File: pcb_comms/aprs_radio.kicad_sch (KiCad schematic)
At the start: 33 parts, among them J5 SMA_CONN, Q1 DTC144EET1G, U3 DRA818V

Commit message: Add UART USB
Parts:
- Q1: footprint SOT50P160X90-3N -> TRANSISTOR_DTC144EET1G:TRANSISTOR_DTC144EET1G
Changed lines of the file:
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@@
 			)
 		)
-		(property "Footprint" "SOT50P160X90-3N"
+		(property "Footprint" "TRANSISTOR_DTC144EET1G:TRANSISTOR_DTC144EET1G"
 			(at 57.15 220.65 0)
 			(effects

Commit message: Update pinout
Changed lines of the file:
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@@
+	)
+	(junction
+		(at 66.04 168.91)
+		(diameter 0)
+		(color 0 0 0 0)
 	)
 	(junction
@@
 	(wire
 		(pts
-			(xy 71.12 168.91) (xy 58.42 168.91)
+			(xy 71.12 168.91) (xy 66.04 168.91)
 		)
 		(stroke
@@
 		(pts
 			(xy 45.72 168.91) (xy 58.42 168.91)
+		)
+		(stroke
+			(width 0)
+			(type default)
+		)
+	)
+	(wire
+		(pts
+			(xy 66.04 168.91) (xy 58.42 168.91)
 		)
 		(stroke
@@
 					(unit 1)
 				)
+			)
+		)
+	)
+	(symbol
+		(lib_id "power:PWR_FLAG")
+		(at 66.04 168.91 0)
+		(unit 1)
+		(exclude_from_sim no)
+		(in_bom yes)
+		(on_board yes)
+		(dnp no)
+		(property "Reference" "#FLG03"
+			(at 66.04 167.005 0)
+			(effects
+				(font
+					(size 1.27 1.27)
+				)
+				(hide yes)
+			)
+		)
+		(property "Value" "PWR_FLAG"
+			(at 66.04 165.1 0)
+			(effects
+				(font
+					(size 1.27 1.27)
+				)
+			)
+		)
+		(property "Footprint" ""
+			(at 66.04 168.91 0)
+			(effects
+				(font
+					(size 1.27 1.27)
+				)
+				(hide yes)
+			)
+		)
+		(property "Datasheet" "~"
+			(at 66.04 168.91 0)
+			(effects
+				(font
+					(size 1.27 1.27)
+				)
+				(hide yes)
+			)
+		)
+		(property "Description" "Special symbol for telling ERC where power comes from"
+			(at 66.04 168.91 0)
+			(effects
+				(font
+					(size 1.27 1.27)
+				)
+				(hide yes)
+			)
+		)
+		(pin "1"
+		)
+		(instances
+			(project ""
+				(path "/ea597178-b44d-4db9-826c-8f86e8d231f0/30ba8b84-3a26-43d9-a2eb-61726928da4d"
+					(reference "#FLG03")
+					(unit 1)
+				)

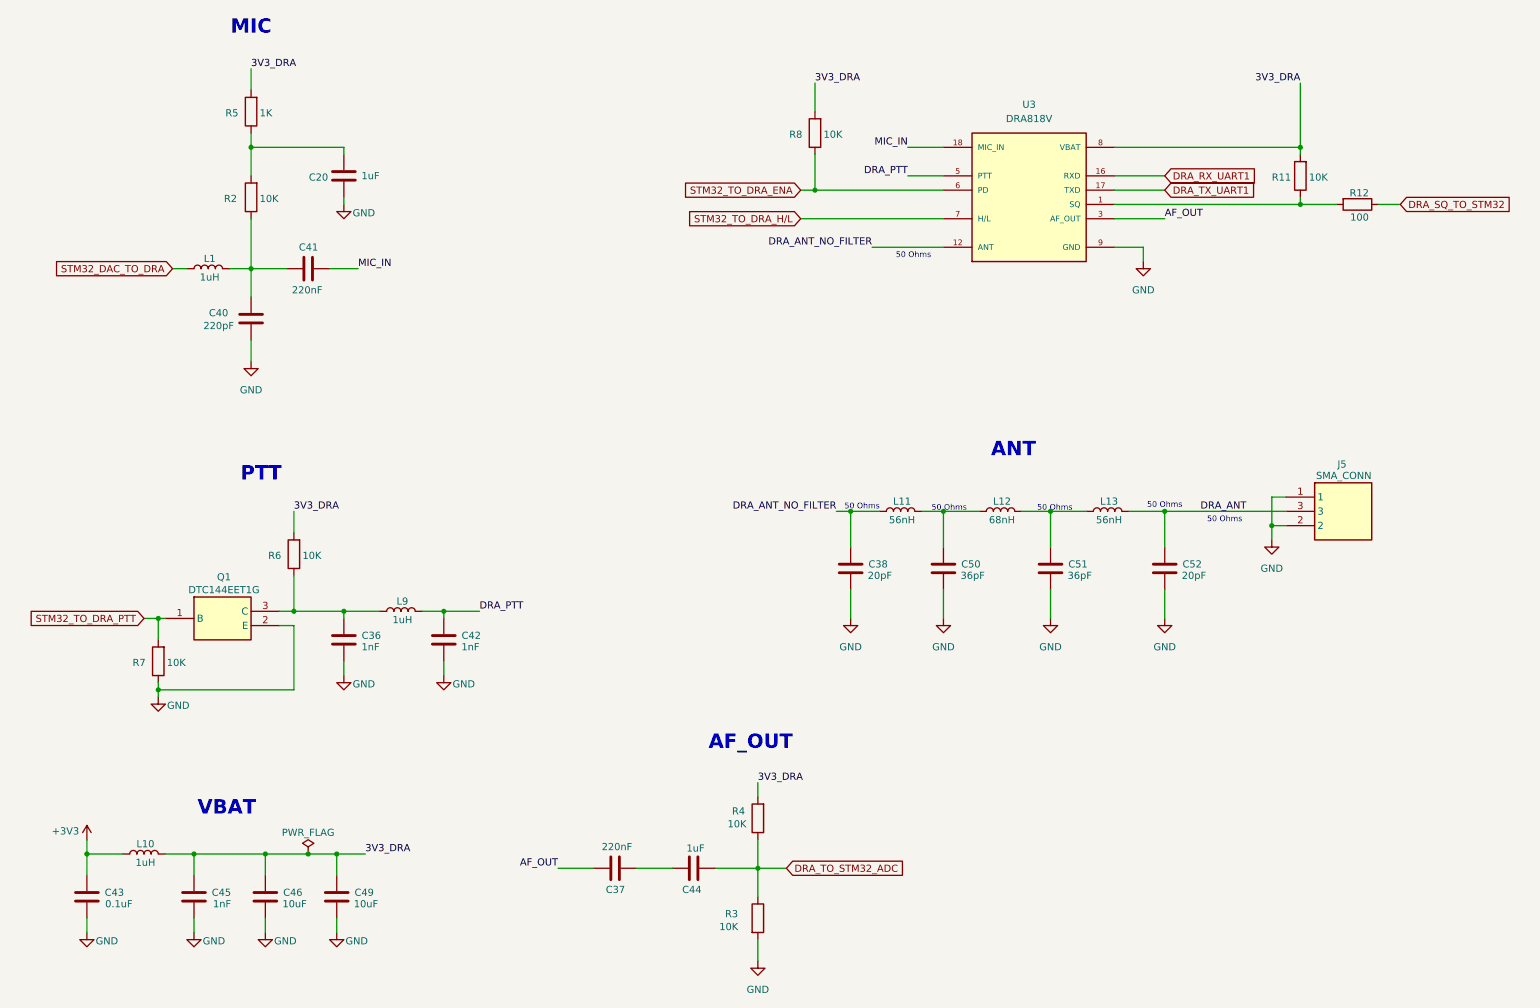
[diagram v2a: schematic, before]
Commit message: Update schematic. Add net classes and JST footprints for aux
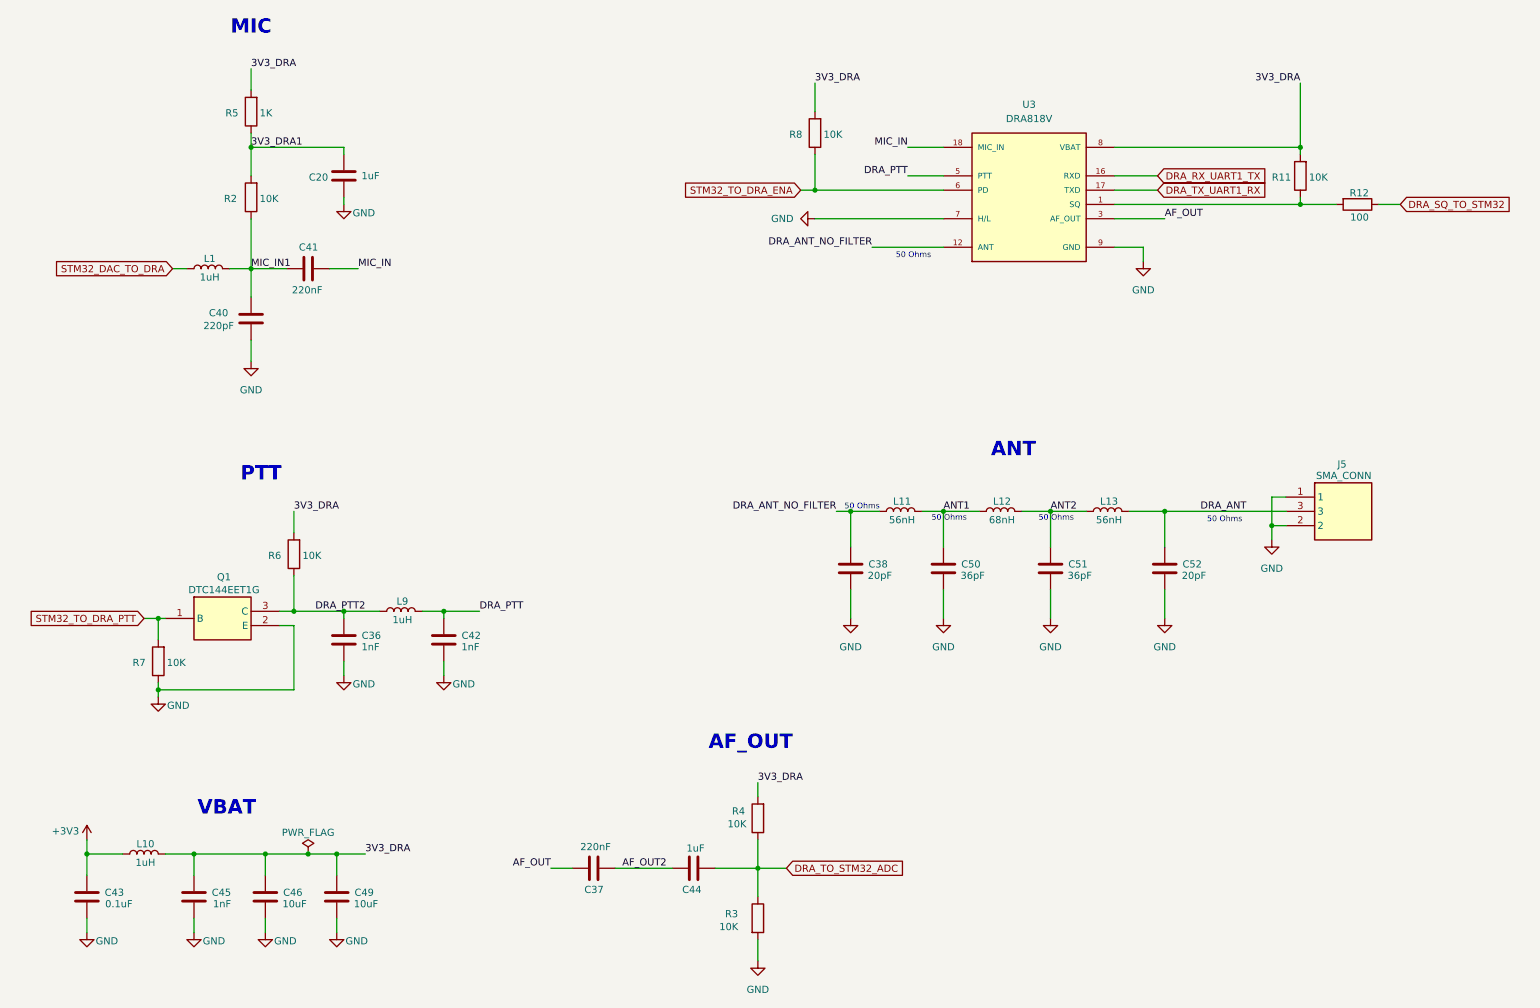
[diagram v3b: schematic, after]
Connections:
- net STM32_TO_DRA_H/L is gone; now on net GND: U3.7 (H/L)
- net MIC_IN1: now reaches C40.1, C41.1, L1.2, R2.1
- net DRA_PTT2: now reaches C36.1, L9.1, Q1.3 (C), R6.1
- net 3V3_DRA1: now reaches C20.1, R2.2, R5.1
- net AF_OUT2: now reaches C37.2, C44.2
- net ANT1: now reaches C50.1, L11.2, L12.1
- net ANT2: now reaches C51.1, L12.2, L13.1
- net DRA_RX_UART1 renamed DRA_RX_UART1_TX
- net DRA_TX_UART1 renamed DRA_TX_UART1_RX
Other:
- moved on the sheet: C37
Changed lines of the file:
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@@
 	(text "50 Ohms"
 		(exclude_from_sim no)
-		(at 180.086 107.442 0)
+		(at 180.086 109.22 0)
 		(effects
 			(font
@@
 	(text "50 Ohms"
 		(exclude_from_sim no)
-		(at 198.882 107.442 0)
-		(effects
-			(font
-				(size 1.016 1.016)
-				(color 255 0 0 1)
-			)
-		)
-	)
-	(text "50 Ohms"
-		(exclude_from_sim no)
-		(at 218.44 106.934 0)
+		(at 199.136 109.22 0)
 		(effects
 			(font
@@
 	(wire
 		(pts
+			(xy 156.21 55.88) (xy 179.07 55.88)
+		)
+		(stroke
+			(width 0)
+			(type default)
+		)
+	)
+	(wire
+		(pts
 			(xy 237.49 110.49) (xy 237.49 113.03)
 		)
@@
 	(wire
 		(pts
-			(xy 110.49 171.45) (xy 116.84 171.45)
+			(xy 109.22 171.45) (xy 113.03 171.45)
 		)
 		(stroke
@@
 	(wire
 		(pts
-			(xy 124.46 171.45) (xy 130.81 171.45)
-		)
-		(stroke
-			(width 0)
-			(type default)
-		)
-	)
-	(wire
-		(pts
 			(xy 153.67 50.8) (xy 156.21 50.8)
 		)
@@
 	(wire
 		(pts
-			(xy 209.55 50.8) (xy 218.44 50.8)
+			(xy 156.21 50.8) (xy 179.07 50.8)
 		)
 		(stroke
@@
 	(wire
 		(pts
-			(xy 156.21 50.8) (xy 179.07 50.8)
+			(xy 242.57 53.34) (xy 248.92 53.34)
 		)
 		(stroke
@@
 	(wire
 		(pts
-			(xy 242.57 53.34) (xy 248.92 53.34)
+			(xy 120.65 171.45) (xy 130.81 171.45)
 		)
 		(stroke
@@
 	(wire
 		(pts
-			(xy 71.12 180.34) (xy 71.12 182.88)
+			(xy 209.55 48.26) (xy 217.17 48.26)
 		)
 		(stroke
@@
 	(wire
 		(pts
-			(xy 153.67 55.88) (xy 179.07 55.88)
+			(xy 71.12 180.34) (xy 71.12 182.88)
 		)
 		(stroke
@@
 	(wire
 		(pts
-			(xy 209.55 48.26) (xy 218.44 48.26)
-		)
-		(stroke
-			(width 0)
-			(type default)
-		)
-	)
-	(wire
-		(pts
 			(xy 90.17 134.62) (xy 90.17 137.16)
 		)
@@
 	(wire
 		(pts
+			(xy 209.55 50.8) (xy 217.17 50.8)
+		)
+		(stroke
+			(width 0)
+			(type default)
+		)
+	)
+	(wire
+		(pts
 			(xy 179.07 107.95) (xy 185.42 107.95)
 		)
@@
 		)
 	)
+	(label "ANT2"
+		(at 198.12 107.95 0)
+		(effects
+			(font
+				(size 1.27 1.27)
+			)
+			(justify left bottom)
+		)
+	)
+	(label "ANT1"
+		(at 179.07 107.95 0)
+		(effects
+			(font
+				(size 1.27 1.27)
+			)
+			(justify left bottom)
+		)
+	)
 	(label "DRA_ANT_NO_FILTER"
 		(at 166.37 60.96 180)
@@
 		)
 	)
+	(label "3V3_DRA1"
+		(at 55.88 43.18 0)
+		(effects
+			(font
+				(size 1.27 1.27)
+			)
+			(justify left bottom)
+		)
+	)
 	(label "DRA_PTT"
 		(at 172.72 48.26 180)
@@
 		)
 	)
+	(label "AF_OUT2"
+		(at 121.92 171.45 0)
+		(effects
+			(font
+				(size 1.27 1.27)
+			)
+			(justify left bottom)
+		)
+	)
 	(label "AF_OUT"
-		(at 110.49 171.45 180)
+		(at 109.22 171.45 180)
 		(effects
 			(font
@@
 		)
 	)
+	(label "DRA_PTT2"
+		(at 67.31 125.73 0)
+		(effects
+			(font
+				(size 1.27 1.27)
+			)
+			(justify left bottom)
+		)
+	)
 	(label "3V3_DRA"
 		(at 63.5 107.95 0)
@@
 		)
 	)
+	(label "MIC_IN1"
+		(at 55.88 64.77 0)
+		(effects
+			(font
+				(size 1.27 1.27)
+			)
+			(justify left bottom)
+		)
+	)
 	(label "AF_OUT"
 		(at 218.44 55.88 0)
@@
 		)
 	)
-	(global_label "DRA_TX_UART1"
-		(shape input)
-		(at 218.44 50.8 0)
-		(fields_autoplaced yes)
-		(effects
-			(font
-				(size 1.27 1.27)
-			)
-			(justify left)
-		)
-		(property "Intersheetrefs" "${INTERSHEET_REFS}"
-			(at 235.0323 50.8 0)
-			(effects
-				(font
-					(size 1.27 1.27)
-				)
-				(justify left)
-				(hide yes)
-			)
-		)
-	)
 	(global_label "STM32_TO_DRA_PTT"
 		(shape input)
@@
 		)
 	)
-	(global_label "STM32_TO_DRA_ENA"
+	(global_label "DRA_RX_UART1_TX"
 		(shape input)
-		(at 153.67 50.8 180)
+		(at 217.17 48.26 0)
 		(fields_autoplaced yes)
 		(effects
@@
 				(size 1.27 1.27)
 			)
-			(justify right)
+			(justify left)
 		)
 		(property "Intersheetrefs" "${INTERSHEET_REFS}"
-			(at 132.2397 50.8 0)
+			(at 237.2094 48.26 0)
 			(effects
 				(font
 					(size 1.27 1.27)
 				)
-				(justify right)
+				(justify left)
 				(hide yes)
 			)
 		)
 	)
-	(global_label "DRA_RX_UART1"
+	(global_label "DRA_TX_UART1_RX"
 		(shape input)
-		(at 218.44 48.26 0)
+		(at 217.17 50.8 0)
 		(fields_autoplaced yes)
 		(effects
@@
 		)
 		(property "Intersheetrefs" "${INTERSHEET_REFS}"
-			(at 235.3347 48.26 0)
+			(at 237.2094 50.8 0)
 			(effects
 				(font
@@
 		)
 	)
-	(global_label "STM32_TO_DRA_H{slash}L"
+	(global_label "STM32_TO_DRA_ENA"
 		(shape input)
-		(at 153.67 55.88 180)
+		(at 153.67 50.8 180)
 		(fields_autoplaced yes)
 		(effects
@@
 		)
 		(property "Intersheetrefs" "${INTERSHEET_REFS}"
-			(at 132.1187 55.88 0)
+			(at 132.2397 50.8 0)
 			(effects
 				(font
@@
 	(symbol
 		(lib_id "power:GND")
+		(at 156.21 55.88 270)
+		(unit 1)
+		(exclude_from_sim no)
+		(in_bom yes)
+		(on_board yes)
+		(dnp no)
+		(fields_autoplaced yes)
+		(property "Reference" "#PWR060"
+			(at 149.86 55.88 0)
+			(effects
+				(font
+					(size 1.27 1.27)
+				)
+				(hide yes)
+			)
+		)
+		(property "Value" "GND"
+			(at 152.4 55.8799 90)
+			(effects
+				(font
+					(size 1.27 1.27)
+				)
+				(justify right)
+			)
+		)
+		(property "Footprint" ""
+			(at 156.21 55.88 0)
+			(effects
+				(font
+					(size 1.27 1.27)
+				)
+				(hide yes)
+			)
+		)
+		(property "Datasheet" ""
+			(at 156.21 55.88 0)
+			(effects
+				(font
+					(size 1.27 1.27)
+				)
+				(hide yes)
+			)
+		)
+		(property "Description" "Power symbol creates a global label with name \"GND\" , ground"
+			(at 156.21 55.88 0)
+			(effects
+				(font
+					(size 1.27 1.27)
+				)
+				(hide yes)
+			)
+		)
+		(pin "1"
+		)
+		(instances
+			(project "pcb_comms_board"
+				(path "/ea597178-b44d-4db9-826c-8f86e8d231f0/30ba8b84-3a26-43d9-a2eb-61726928da4d"
+					(reference "#PWR060")
+					(unit 1)
+				)
+			)
+		)
+	)
+	(symbol
+		(lib_id "power:GND")
 		(at 214.63 63.5 0)
 		(unit 1)
@@
 	(symbol
 		(lib_id "Device:C")
-		(at 120.65 171.45 90)
+		(at 116.84 171.45 90)
 		(unit 1)
 		(exclude_from_sim no)
@@
 		(dnp no)
 		(property "Reference" "C37"
-			(at 122.428 175.26 90)
+			(at 118.618 175.26 90)
 			(effects
 				(font
@@
 		)
 		(property "Value" "220nF"
-			(at 123.698 167.64 90)
+			(at 119.888 167.64 90)
 			(effects
 				(font
@@
 		)
 		(property "Footprint" "Capacitor_SMD:C_0805_2012Metric_Pad1.18x1.45mm_HandSolder"
-			(at 124.46 170.4848 0)
+			(at 120.65 170.4848 0)
 			(effects
 				(font
@@
 		)
 		(property "Datasheet" "~"
-			(at 120.65 171.45 0)
+			(at 116.84 171.45 0)
 			(effects
 				(font
@@
 		)
 		(property "Description" "Unpolarized capacitor"
-			(at 120.65 171.45 0)
+			(at 116.84 171.45 0)
 			(effects
 				(font
@@
 		)
 		(property "KLC_S3.3" ""
-			(at 120.65 171.45 90)
+			(at 116.84 171.45 90)
 			(effects
 				(font
@@
 		)
 		(property "KLC_S4.1" ""
-			(at 120.65 171.45 90)
+			(at 116.84 171.45 90)
 			(effects
 				(font

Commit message: Version 1.1
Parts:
- removed J5: SMA_CONN, SMA_ANTENNA_CONSMA002-SMD-G:SMA_ANTENNA_CONSMA002-SMD-G, symbol SMA_ANTENNA_CONSMA002-SMD-G:CONSMA002-SMD-G
- added J4: SMA_CONNECTOR, SMA_ANTENNA_VERTICAL:LPRS_SMA_CONNECTOR, symbol SMA_CONNECTOR:SMA_CONNECTOR
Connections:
- net DRA_ANT: now also J4.1
- net GND: now also J4.G1, J4.G2, J4.G3, J4.G4
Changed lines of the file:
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@@
 	)
 	(junction
-		(at 237.49 110.49)
-		(diameter 0)
-		(color 0 0 0 0)
-	)
-	(junction
 		(at 39.37 139.7)
 		(diameter 0)
@@
 	(wire
 		(pts
-			(xy 240.03 110.49) (xy 237.49 110.49)
+			(xy 237.49 110.49) (xy 241.3 110.49)
 		)
 		(stroke
@@
 	(wire
 		(pts
-			(xy 218.44 107.95) (xy 240.03 107.95)
+			(xy 218.44 107.95) (xy 241.3 107.95)
 		)
 		(stroke
@@
 	(wire
 		(pts
-			(xy 240.03 105.41) (xy 237.49 105.41)
-		)
-		(stroke
-			(width 0)
-			(type default)
-		)
-	)
-	(wire
-		(pts
-			(xy 237.49 105.41) (xy 237.49 110.49)
-		)
-		(stroke
-			(width 0)
-			(type default)
-		)
-	)
-	(wire
-		(pts
 			(xy 63.5 119.38) (xy 63.5 125.73)
 		)
@@
 	)
 	(symbol
-		(lib_id "SMA_ANTENNA_CONSMA002-SMD-G:CONSMA002-SMD-G")
-		(at 240.03 105.41 0)
-		(unit 1)
-		(exclude_from_sim no)
-		(in_bom yes)
-		(on_board yes)
-		(dnp no)
-		(property "Reference" "J5"
-			(at 249.174 99.568 0)
-			(effects
-				(font
-					(size 1.27 1.27)
-				)
-				(justify left)
-			)
-		)
-		(property "Value" "SMA_CONN"
-			(at 245.364 101.6 0)
-			(effects
-				(font
-					(size 1.27 1.27)
-				)
-				(justify left)
-			)
-		)
-		(property "Footprint" "SMA_ANTENNA_CONSMA002-SMD-G:SMA_ANTENNA_CONSMA002-SMD-G"
-			(at 256.54 200.33 0)
-			(effects
-				(font
-					(size 1.27 1.27)
-				)
-				(justify left top)
-				(hide yes)
-			)
-		)
-		(property "Datasheet" "https://www.te.com/commerce/DocumentDelivery/DDEController?Action=srchrtrv&DocNm=C-CONSMA002-SMD-X-X&DocType=Customer%20Drawing&DocLang=English&DocFormat=pdf&PartCntxt=CONSMA002-SMD-G"
-			(at 256.54 300.33 0)
-			(effects
-				(font
-					(size 1.27 1.27)
-				)
-				(justify left top)
-				(hide yes)
-			)
-		)
-		(property "Description" "SMA Connector Receptacle, Female Socket 50 Ohms Surface Mount, Right Angle Solder"
-			(at 240.03 105.41 0)
-			(effects
-				(font
-					(size 1.27 1.27)
-				)
-				(hide yes)
-			)
-		)
-		(property "Height" "10.9"
-			(at 256.54 500.33 0)
-			(effects
-				(font
-					(size 1.27 1.27)
-				)
-				(justify left top)
-				(hide yes)
-			)
-		)
-		(property "Manufacturer_Name" "TE Connectivity"
-			(at 256.54 600.33 0)
-			(effects
-				(font
-					(size 1.27 1.27)
-				)
-				(justify left top)
-				(hide yes)
-			)
-		)
-		(property "Manufacturer_Part_Number" "CONSMA002-SMD-G"
-			(at 256.54 700.33 0)
-			(effects
-				(font
-					(size 1.27 1.27)
-				)
-				(justify left top)
-				(hide yes)
-			)
-		)
-		(property "Mouser Part Number" "712-CONSMA002-SMD-G"
-			(at 256.54 800.33 0)
-			(effects
-				(font
-					(size 1.27 1.27)
-				)
-				(justify left top)
-				(hide yes)
-			)
-		)
-		(property "Mouser Price/Stock" "https://www.mouser.co.uk/ProductDetail/TE-Connectivity-Linx-Technologies/CONSMA002-SMD-G?qs=W0r2Z67sYIIuXfZnKPZ6sQ%3D%3D"
-			(at 256.54 900.33 0)
-			(effects
-				(font
-					(size 1.27 1.27)
-				)
-				(justify left top)
-				(hide yes)
-			)
-		)
-		(property "Arrow Part Number" "CONSMA002-SMD-G"
-			(at 256.54 1000.33 0)
-			(effects
-				(font
-					(size 1.27 1.27)
-				)
-				(justify left top)
-				(hide yes)
-			)
-		)
-		(property "Arrow Price/Stock" "https://www.arrow.com/en/products/consma002-smd-g/te-connectivity?utm_currency=USD&region=nac"
-			(at 256.54 1100.33 0)
-			(effects
-				(font
-					(size 1.27 1.27)
-				)
-				(justify left top)
-				(hide yes)
-			)
-		)
-		(pin "3"
-		)
-		(pin "2"
-		)
-		(pin "1"
-		)
-		(instances
-			(project "pcb_comms_board"
-				(path "/ea597178-b44d-4db9-826c-8f86e8d231f0/30ba8b84-3a26-43d9-a2eb-61726928da4d"
-					(reference "J5")
-					(unit 1)
-				)
-			)
-		)
-	)
-	(symbol
 		(lib_id "Device:C")
 		(at 72.39 48.26 0)
@@
 					(unit 1)
 				)
+			)
+		)
+	)
+	(symbol
+		(lib_id "SMA_CONNECTOR:SMA_CONNECTOR")
+		(at 243.84 107.95 0)
+		(mirror y)
+		(unit 1)
+		(exclude_from_sim no)
+		(in_bom yes)
+		(on_board yes)
+		(dnp no)
+		(property "Reference" "J4"
+			(at 244.9195 101.6 0)
+			(effects
+				(font
+					(size 1.27 1.27)
+				)
+			)
+		)
+		(property "Value" "SMA_CONNECTOR"
+			(at 244.9195 104.14 0)
+			(effects
+				(font
+					(size 1.27 1.27)
+				)
+			)
+		)
+		(property "Footprint" "SMA_ANTENNA_VERTICAL:LPRS_SMA_CONNECTOR"
+			(at 243.84 107.95 0)
+			(effects
+				(font
+					(size 1.27 1.27)
+				)
+				(justify bottom)
+				(hide yes)
+			)
+		)
+		(property "Datasheet" ""
+			(at 243.84 107.95 0)
+			(effects
+				(font
+					(size 1.27 1.27)
+				)
+				(hide yes)
+			)
+		)
+		(property "Description" ""
+			(at 243.84 107.95 0)
+			(effects
+				(font
+					(size 1.27 1.27)
+				)
+				(hide yes)
+			)
+		)
+		(property "MF" "LPRS"
+			(at 243.84 107.95 0)
+			(effects
+				(font
+					(size 1.27 1.27)
+				)
+				(justify bottom)
+				(hide yes)
+			)
+		)
+		(property "MAXIMUM_PACKAGE_HEIGHT" "8.3 mm"
+			(at 243.84 107.95 0)
+			(effects
+				(font
+					(size 1.27 1.27)
+				)
+				(justify bottom)
+				(hide yes)
+			)
+		)
+		(property "Package" "None"
+			(at 243.84 107.95 0)
+			(effects
+				(font
+					(size 1.27 1.27)
+				)
+				(justify bottom)
+				(hide yes)
+			)
+		)
+		(property "Price" "None"
+			(at 243.84 107.95 0)
+			(effects
+				(font
+					(size 1.27 1.27)
+				)
+				(justify bottom)
+				(hide yes)
+			)
+		)
+		(property "Check_prices" "https://www.snapeda.com/parts/SMA%20CONNECTOR/LPRS/view-part/?ref=eda"
+			(at 243.84 107.95 0)
+			(effects
+				(font
+					(size 1.27 1.27)
+				)
+				(justify bottom)
+				(hide yes)
+			)
+		)
+		(property "STANDARD" "Manufacturer Recommendations"
+			(at 243.84 107.95 0)
+			(effects
+				(font
+					(size 1.27 1.27)
+				)
+				(justify bottom)
+				(hide yes)
+			)
+		)
+		(property "PARTREV" "1.3"
+			(at 243.84 107.95 0)
+			(effects
+				(font
+					(size 1.27 1.27)
+				)
+				(justify bottom)
+				(hide yes)
+			)
+		)
+		(property "SnapEDA_Link" "https://www.snapeda.com/parts/SMA%20CONNECTOR/LPRS/view-part/?ref=snap"
+			(at 243.84 107.95 0)
+			(effects
+				(font
+					(size 1.27 1.27)
+				)
+				(justify bottom)
+				(hide yes)
+			)
+		)
+		(property "MP" "SMA CONNECTOR"
+			(at 243.84 107.95 0)
+			(effects
+				(font
+					(size 1.27 1.27)
+				)
+				(justify bottom)
+				(hide yes)
+			)
+		)
+		(property "Description_1" "RF Coaxial Straight SMA Connector"
+			(at 243.84 107.95 0)
+			(effects
+				(font
+					(size 1.27 1.27)
+				)
+				(justify bottom)
+				(hide yes)
+			)
+		)
+		(property "Availability" "In Stock"
+			(at 243.84 107.95 0)
+			(effects
+				(font
+					(size 1.27 1.27)
+				)
+				(justify bottom)
+				(hide yes)
+			)
+		)
+		(property "MANUFACTURER" "LPRS"
+			(at 243.84 107.95 0)
+			(effects
+				(font
+					(size 1.27 1.27)
+				)
+				(justify bottom)
+				(hide yes)
+			)
+		)
+		(pin "G2"
+		)
+		(pin "G3"
+		)
+		(pin "1"
+		)
+		(pin "G1"
+		)
+		(pin "G4"
+		)
+		(instances
+			(project "pcb_comms_board"
+				(path "/ea597178-b44d-4db9-826c-8f86e8d231f0/30ba8b84-3a26-43d9-a2eb-61726928da4d"
+					(reference "J4")
+					(unit 1)
+				)

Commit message: PCB v2.1
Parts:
- L1, L10, L9: footprint Inductor_SMD:L_0805_2012Metric_Pad1.05x1.20mm_HandSolder -> Inductor_SMD:L_1210_3225Metric_Pad1.42x2.65mm_HandSolder
- R12: value 100 -> 100R
